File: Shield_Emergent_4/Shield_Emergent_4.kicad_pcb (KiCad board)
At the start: 4 copper layers, 27 x 36 mm, 37 parts, among them J1 TF31-18S-0.5SH_800_, J2 Conn_01x04_Socket, J3 TF31-18S-0.5SH_800_, J4 Conn_01x05, J5 Conn_01x02_Socket, J6 Conn_01x02_Socket, J7 Conn_01x05, J8 Conn_02x05_Odd_Even, U3 SP3012-06UTG, U4 SP3012-06UTG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

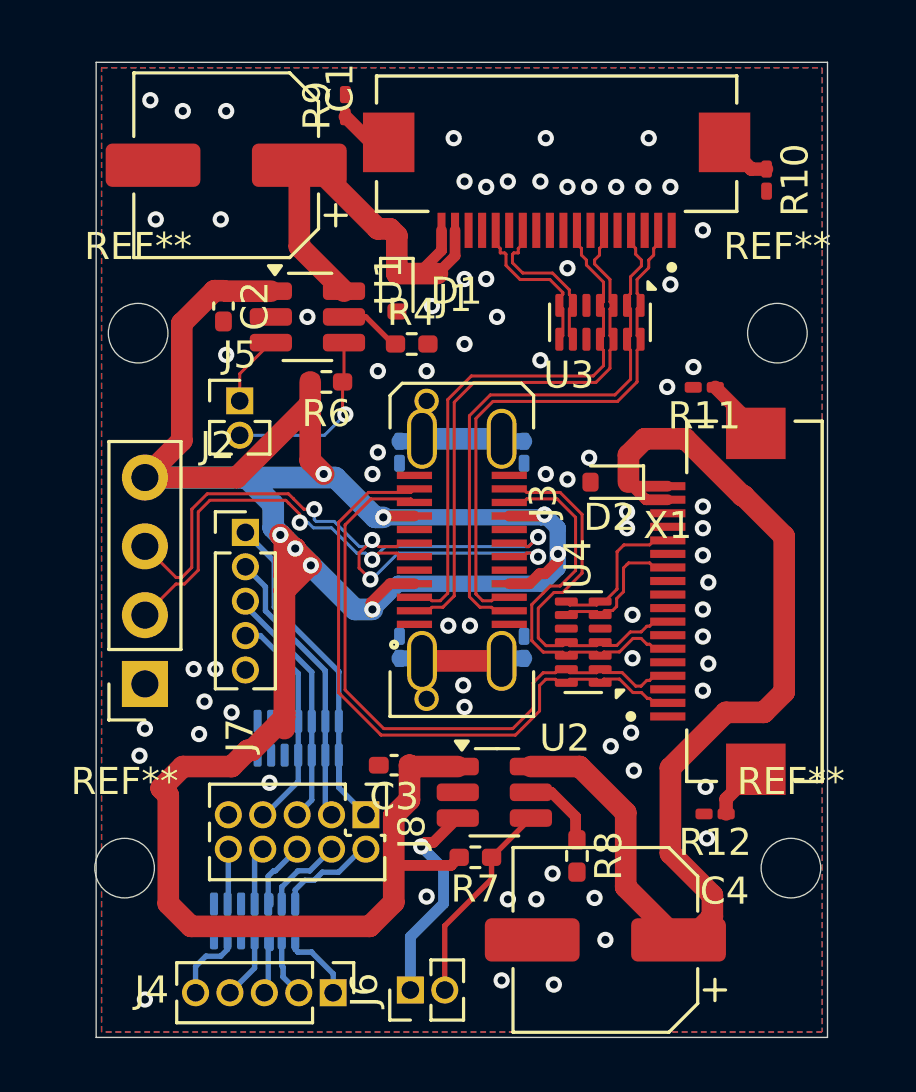
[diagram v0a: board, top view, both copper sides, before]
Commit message: v1.0 diffpairs routed correctly
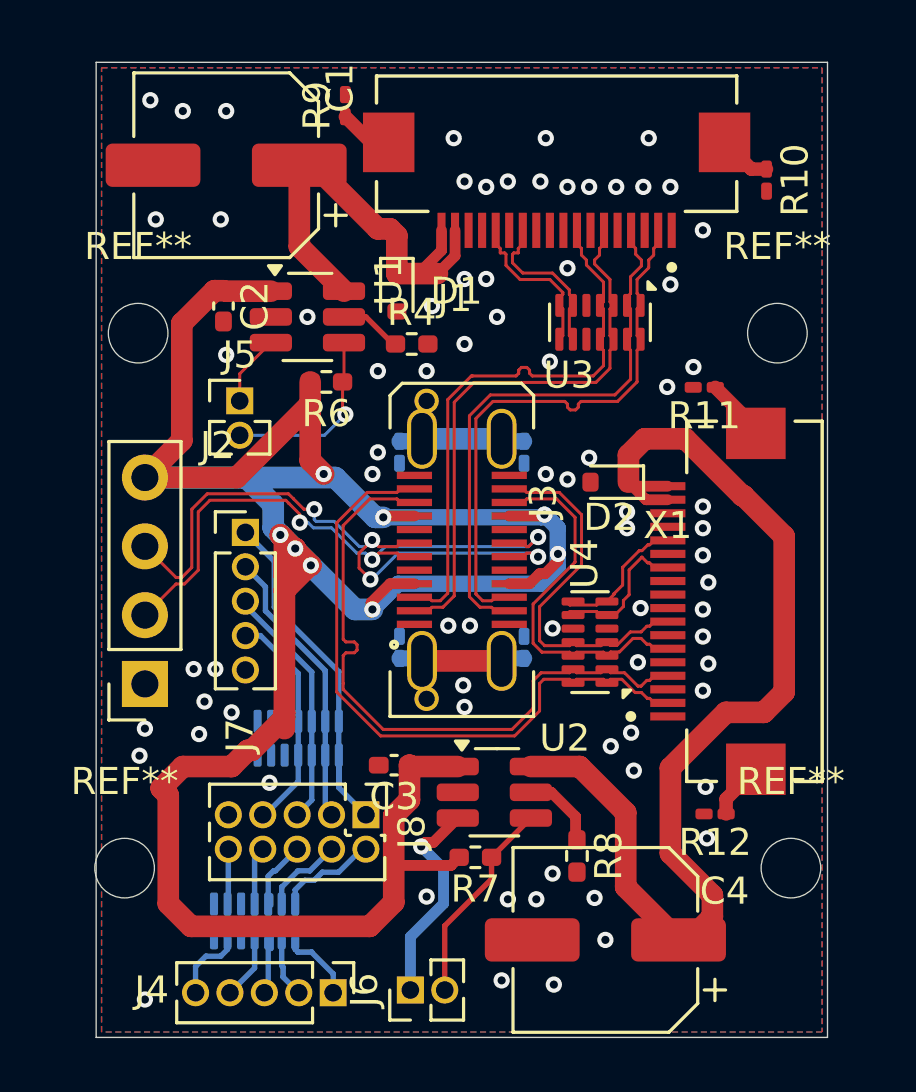
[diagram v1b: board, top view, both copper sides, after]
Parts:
- moved U4 0.25 mm to (18.2, 21.4)
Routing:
- net RX2-: track 23.6 -> 24.6 mm
- net GND: vias 75 -> 76
